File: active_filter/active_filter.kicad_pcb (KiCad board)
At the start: 2 copper layers, 36.1 x 21.1 mm, 15 parts, among them J1 Screw_Terminal_01x03, J2 Screw_Terminal_01x02, U1 ADA4062-2

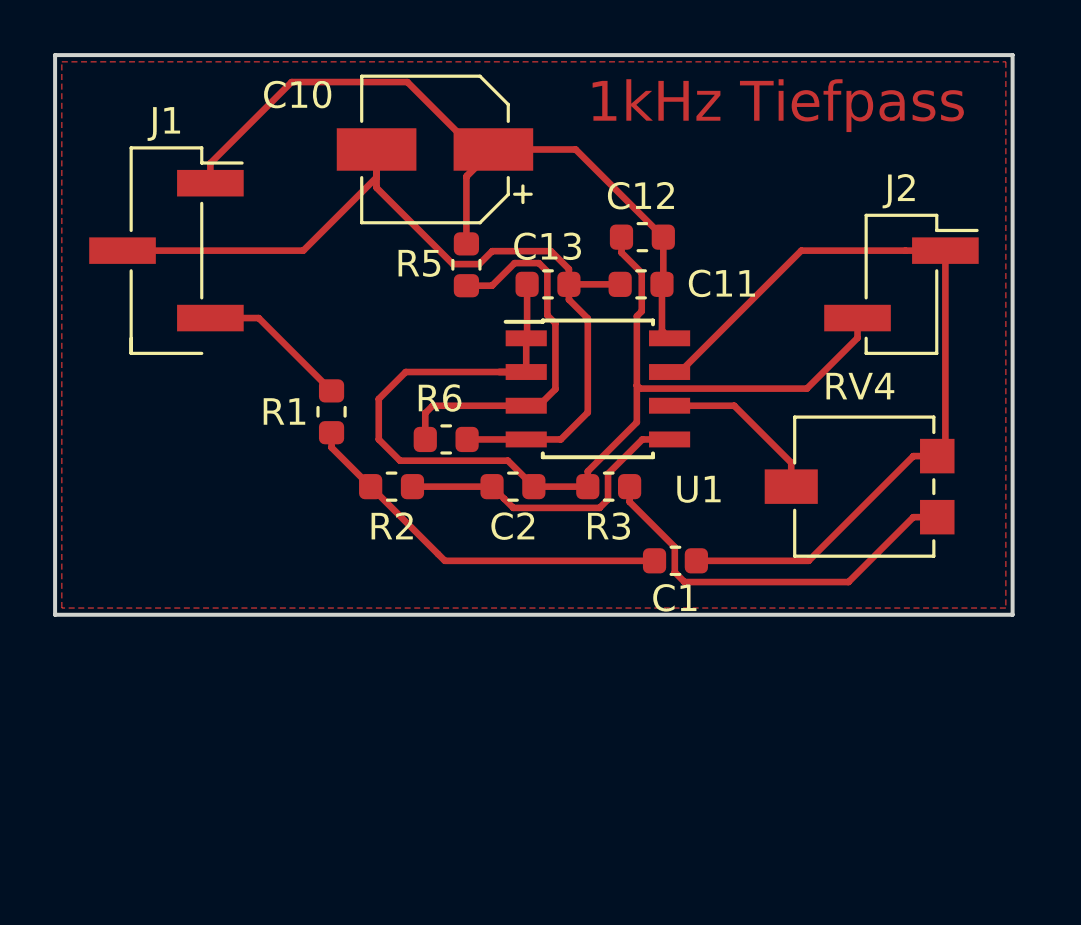
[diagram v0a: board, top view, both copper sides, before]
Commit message: changed parts checked design rules
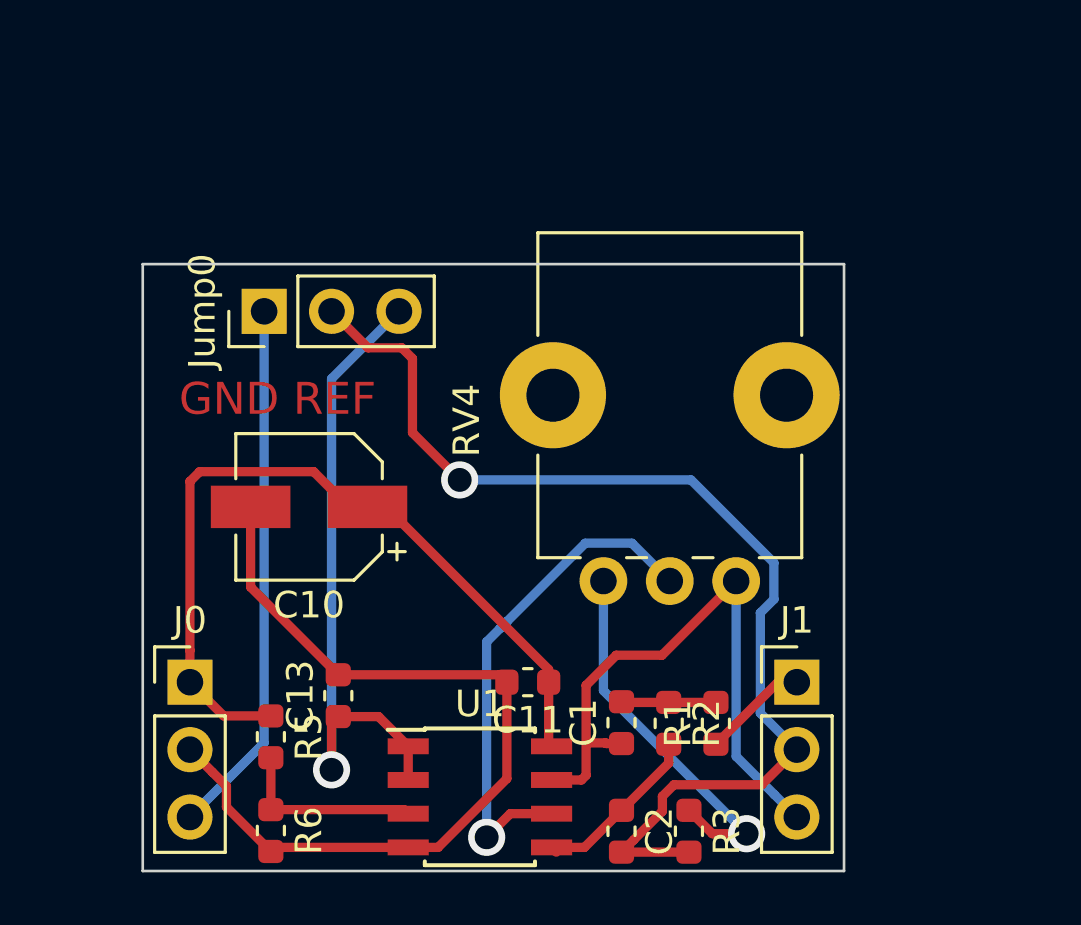
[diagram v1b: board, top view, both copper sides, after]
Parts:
- removed C12: 100n, default-footprints:C_0603_1608Metric
- removed J2: Screw_Terminal_01x02, default-footprints:PinHeader_1x02_P2.54mm_Vertical_SMD_Pin1Right
- added J0: Conn_01x03_MountingPin, default-footprints:PinHeader_1x03_P2.54mm_Vertical, F.Cu at (22.9, 45.5)
- added Jump0: Jumper_3_Bridged12, default-footprints:PinHeader_1x03_P2.54mm_Vertical, F.Cu at (25.7, 31.5)
- J1: value Screw_Terminal_01x03 -> Conn_01x03_MountingPin; footprint default-footprints:PinHeader_1x03_P2.54mm_Vertical_SMD_Pin1Right -> default-footprints:PinHeader_1x03_P2.54mm_Vertical
- RV4: footprint default-footprints:Potentiometer_Vishay_TS53YL_Vertical -> default-footprints:Potentiometer_Bourns_PTV09A-1_Single_Vertical
- moved J1 28.8 mm to (45.7, 45.5)
- moved R5 19.2 mm to (25.9, 47.5)
- moved R1 18.6 mm to (42.7, 47.0), turned to 90 degrees
- moved C13 17.4 mm to (28.4, 46.0), turned to 90 degrees
- moved R6 16.1 mm to (25.9, 51.1), turned to 270 degrees
- moved U1 16.0 mm to (33.8, 49.8)
- moved C11 15.6 mm to (35.6, 45.5)
- moved C10 14.3 mm to (27.3, 38.9)
- moved R2 13.7 mm to (40.9, 47.0), turned to 270 degrees
- moved C2 13.6 mm to (39.1, 51.1), turned to 270 degrees
- moved R3 13.3 mm to (41.7, 51.1), turned to 270 degrees
- moved C1 6.43 mm to (39.1, 47.0), turned to 90 degrees
- moved RV4 5.99 mm to (43.4, 41.7), turned to 90 degrees
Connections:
- C10 pad 1: +10V -> VCC
- C10 pad 2: GND -> VEE
- C11 pad 1: +10V -> VCC
- C11 pad 2: GND -> VEE
- C13 pad 2: GND -> VEE
- C2 pad 2: REF -> COM
- J1 pad 1: +10V -> IN
- J1 pad 2: GND -> COM
- J1 pad 3: IN -> OUT
- R3 pad 2: REF -> COM
- R5 pad 1: +10V -> VCC
- R6 pad 2: GND -> VEE
- U1 pad 4: GND -> VEE
- U1 pad 8: +10V -> VCC
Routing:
- net COM: track 0.00 -> 41.1 mm, vias 0 -> 1
- net VEE: track 0.00 -> 32.9 mm
- net +10V: track 31.3 -> 0.00 mm
- net VCC: track 0.00 -> 30.8 mm
- net REF: track 41.7 -> 24.8 mm, vias 0 -> 1
- net GND: track 35.2 -> 20.2 mm
- net Net-(RV4-Pad2): track 6.37 -> 19.6 mm, vias 0 -> 1
- net Net-(C1-Pad2): track 14.5 -> 3.57 mm
- net OUT: track 30.9 -> 23.2 mm
- net Net-(R5-Pad2): track 14.6 -> 7.19 mm
- net Net-(C2-Pad1): track 11.7 -> 6.69 mm
- net IN: track 5.70 -> 4.02 mm
- net Net-(R3-Pad1): track 15.0 -> 14.3 mm, vias 0 -> 1
- removed copper zone on F.Cu, net GND
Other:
- board size 36.1 x 21.1 mm -> 26.4 x 22.9 mm
- net class Default: clearance 0.2 -> 0.35; trace_width 0.25 -> 0.35; via_dia 0.8 -> 1.4; via_drill 0.4 -> 0.9
- rule pad_to_mask_clearance: 0.2 -> 0
- rule trace_clearance: 0.2 -> 0.35
- rule trace_min: 0.2 -> 0.4
- rule via_min_drill: 0.3 -> 0.9
- rule via_min_size: 0.4 -> 1.2
- board text added: "GND REF"
- board text removed: "1kHz Tiefpass"

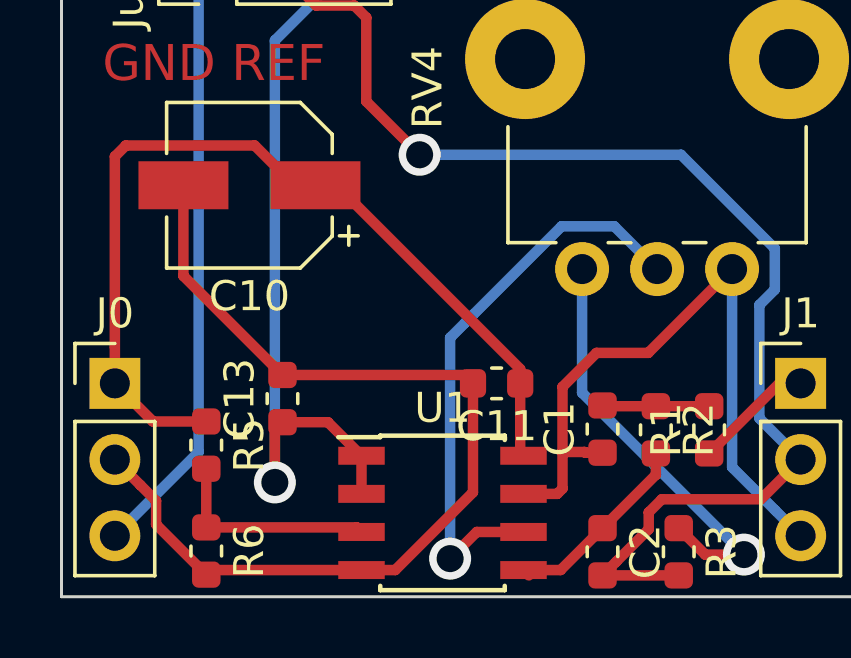
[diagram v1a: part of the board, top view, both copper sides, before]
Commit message: changed critical via
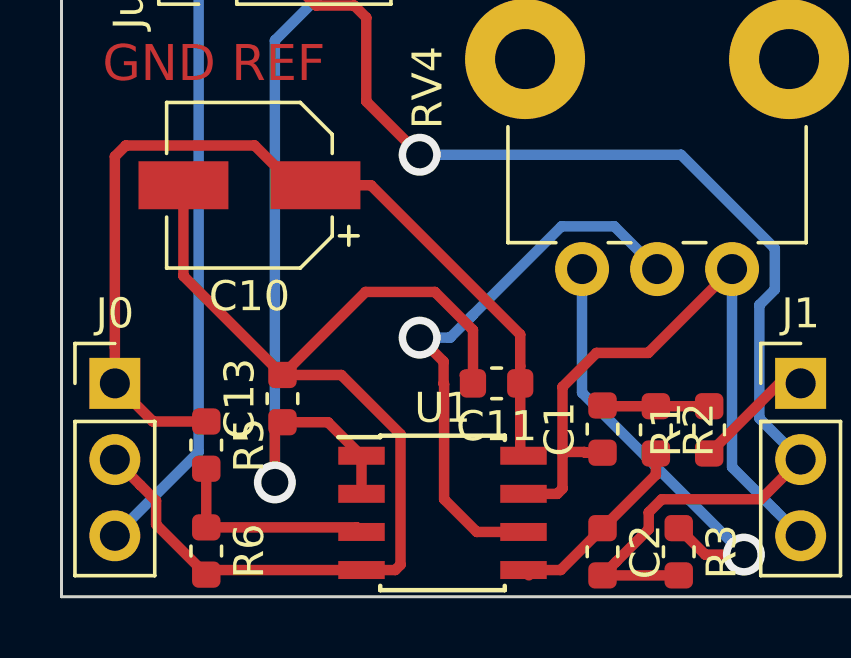
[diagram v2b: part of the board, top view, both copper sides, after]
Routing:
- net VEE: track 32.9 -> 38.7 mm
- net VCC: track 30.8 -> 31.5 mm
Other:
- rule via_min_size: 1.2 -> 1.905
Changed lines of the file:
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@@
     (thickness 1.6)
     (drawings 5)
-    (tracks 96)
+    (tracks 108)
     (zones 0)
     (modules 15)
@@
     (47 F.CrtYd user)
     (48 B.Fab user)
-    (49 F.Fab user)
+    (49 F.Fab user hide)
   )
   (setup
@@
     (via_size 1.4)
     (via_drill 0.9)
-    (via_min_size 1.2)
+    (via_min_size 1.905)
     (via_min_drill 0.9)
     (uvia_size 0.3)
@@
   (gr_line (start 21.082 52.578) (end 47.498 52.578) (layer Edge.Cuts) (width 0.1))
   (via (at 33.02 37.846) (size 1.4) (drill 0.9) (layers F.Cu B.Cu) (net 11))
-  (via (at 34.036 51.308) (size 1.4) (drill 0.9) (layers F.Cu B.Cu) (net 5))
+  (via (at 33.02 43.942) (size 1.4) (drill 0.9) (layers F.Cu B.Cu) (net 5))
   (via (at 28.194 48.768) (size 1.4) (drill 0.9) (layers F.Cu B.Cu) (net 1))
   (segment (start 29.9645 46.7615) (end 31.082 47.879) (width 0.35) (layer F.Cu) (net 1))
@@
   (segment (start 25.146 38.862) (end 25.146 41.8845) (width 0.35) (layer F.Cu) (net 3))
   (segment (start 34.5185 45.1865) (end 34.798 45.466) (width 0.35) (layer F.Cu) (net 3))
-  (segment (start 28.448 45.1865) (end 34.5185 45.1865) (width 0.35) (layer F.Cu) (net 3))
-  (segment (start 32.207 51.689) (end 31.082 51.689) (width 0.35) (layer F.Cu) (net 3))
-  (segment (start 34.798 49.098) (end 32.207 51.689) (width 0.35) (layer F.Cu) (net 3))
-  (segment (start 34.798 45.466) (end 34.798 49.098) (width 0.35) (layer F.Cu) (net 3))
   (segment (start 26.0605 51.689) (end 25.908 51.8415) (width 0.35) (layer F.Cu) (net 3))
   (segment (start 31.082 51.689) (end 26.0605 51.689) (width 0.35) (layer F.Cu) (net 3))
@@
   (segment (start 24.235001 49.381001) (end 23.709999 48.855999) (width 0.35) (layer F.Cu) (net 3))
   (segment (start 25.908 51.8415) (end 24.235001 50.168501) (width 0.35) (layer F.Cu) (net 3))
+  (segment (start 34.798 45.466) (end 34.798 43.688) (width 0.35) (layer F.Cu) (net 3))
+  (segment (start 34.798 43.688) (end 33.528 42.418) (width 0.35) (layer F.Cu) (net 3))
+  (segment (start 31.2165 42.418) (end 28.448 45.1865) (width 0.35) (layer F.Cu) (net 3))
+  (segment (start 33.528 42.418) (end 31.2165 42.418) (width 0.35) (layer F.Cu) (net 3))
+  (segment (start 32.207 51.689) (end 31.082 51.689) (width 0.35) (layer F.Cu) (net 3))
+  (segment (start 30.409502 45.1865) (end 32.382001 47.158999) (width 0.35) (layer F.Cu) (net 3))
+  (segment (start 32.382001 51.513999) (end 32.207 51.689) (width 0.35) (layer F.Cu) (net 3))
+  (segment (start 32.382001 47.158999) (end 32.382001 51.513999) (width 0.35) (layer F.Cu) (net 3))
+  (segment (start 28.448 45.1865) (end 30.409502 45.1865) (width 0.35) (layer F.Cu) (net 3))
   (segment (start 36.66 51.867) (end 36.482 51.689) (width 0.35) (layer F.Cu) (net 4))
   (segment (start 40.894 48.514) (end 39.116 50.292) (width 0.35) (layer F.Cu) (net 4))
@@
   (segment (start 40.934 41.656) (end 39.508999 40.230999) (width 0.35) (layer B.Cu) (net 5))
   (segment (start 34.036 43.944998) (end 34.798 43.182998) (width 0.35) (layer B.Cu) (net 5))
-  (segment (start 34.036 51.308) (end 34.036 43.944998) (width 0.35) (layer B.Cu) (net 5))
   (segment (start 37.749999 40.230999) (end 34.798 43.182998) (width 0.35) (layer B.Cu) (net 5))
   (segment (start 34.798 43.182998) (end 34.544 43.436998) (width 0.35) (layer B.Cu) (net 5))
-  (segment (start 34.925 50.419) (end 34.036 51.308) (width 0.35) (layer F.Cu) (net 5))
   (segment (start 36.482 50.419) (end 34.925 50.419) (width 0.35) (layer F.Cu) (net 5))
+  (segment (start 33.818492 44.740492) (end 33.02 43.942) (width 0.35) (layer F.Cu) (net 5))
+  (segment (start 33.818492 45.476454) (end 33.818492 44.740492) (width 0.35) (layer F.Cu) (net 5))
+  (segment (start 33.83549 45.493452) (end 33.818492 45.476454) (width 0.35) (layer F.Cu) (net 5))
+  (segment (start 33.83549 49.32949) (end 33.83549 45.493452) (width 0.35) (layer F.Cu) (net 5))
+  (segment (start 34.925 50.419) (end 33.83549 49.32949) (width 0.35) (layer F.Cu) (net 5))
+  (segment (start 34.012947 43.944998) (end 34.036 43.944998) (width 0.35) (layer B.Cu) (net 5))
+  (segment (start 34.009949 43.942) (end 34.012947 43.944998) (width 0.35) (layer B.Cu) (net 5))
+  (segment (start 33.02 43.942) (end 34.009949 43.942) (width 0.35) (layer B.Cu) (net 5))
   (segment (start 43.434 41.656) (end 40.64 44.45) (width 0.35) (layer F.Cu) (net 6))
   (segment (start 37.782001 48.973999) (end 37.607 49.149) (width 0.35) (layer F.Cu) (net 6))
@@
   (segment (start 44.870001 49.696001) (end 45.72 50.546) (width 0.35) (layer B.Cu) (net 6))
   (segment (start 43.434 41.656) (end 43.434 48.26) (width 0.35) (layer B.Cu) (net 6))
-  (segment (start 36.373 44.989) (end 36.373 45.466) (width 0.35) (layer F.Cu) (net 7))
-  (segment (start 30.246 38.862) (end 36.373 44.989) (width 0.35) (layer F.Cu) (net 7))
-  (segment (start 29.546 38.862) (end 30.246 38.862) (width 0.35) (layer F.Cu) (net 7))
   (segment (start 36.373 47.77) (end 36.482 47.879) (width 0.35) (layer F.Cu) (net 7))
   (segment (start 36.373 45.466) (end 36.373 47.77) (width 0.35) (layer F.Cu) (net 7))
@@
   (segment (start 28.846 38.862) (end 27.520999 37.536999) (width 0.35) (layer F.Cu) (net 7))
   (segment (start 29.546 38.862) (end 28.846 38.862) (width 0.35) (layer F.Cu) (net 7))
+  (segment (start 29.546 38.862) (end 31.396 38.862) (width 0.35) (layer F.Cu) (net 7))
+  (segment (start 36.373 43.839) (end 36.373 44.891) (width 0.35) (layer F.Cu) (net 7))
+  (segment (start 31.396 38.862) (end 36.373 43.839) (width 0.35) (layer F.Cu) (net 7))
+  (segment (start 36.373 44.891) (end 36.373 45.466) (width 0.35) (layer F.Cu) (net 7))
   (segment (start 45.009 45.466) (end 42.672 47.803) (width 0.35) (layer F.Cu) (net 8))
   (segment (start 45.72 45.466) (end 45.009 45.466) (width 0.35) (layer F.Cu) (net 8))

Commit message: updated pcb and bom
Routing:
- net COM: track 41.1 -> 0.00 mm, vias 1 -> 3
- net OUT: track 23.2 -> 24.5 mm
- added copper zone on B.Cu, net COM
- added copper zone on F.Cu, net COM
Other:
- net class Default: trace_width 0.35 -> 0.4; via_dia 1.4 -> 1.8
- rule via_min_size: 1.905 -> 1.8
